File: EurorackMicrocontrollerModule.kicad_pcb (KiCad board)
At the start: 2 copper layers, 17.8 x 109.2 mm, 43 parts, among them J1 Teensy4.0_Pins_Right, J2 Teensy4.0_Pins_Left, J3 Conn_01x24_Male, J4 Conn_02x05_Counter_Clockwise, J5 Teensy4.0_Pins_Top, U1 PCM1754DBQ, U2 PCM1808PW, U3 AZ1117H2-ADJ

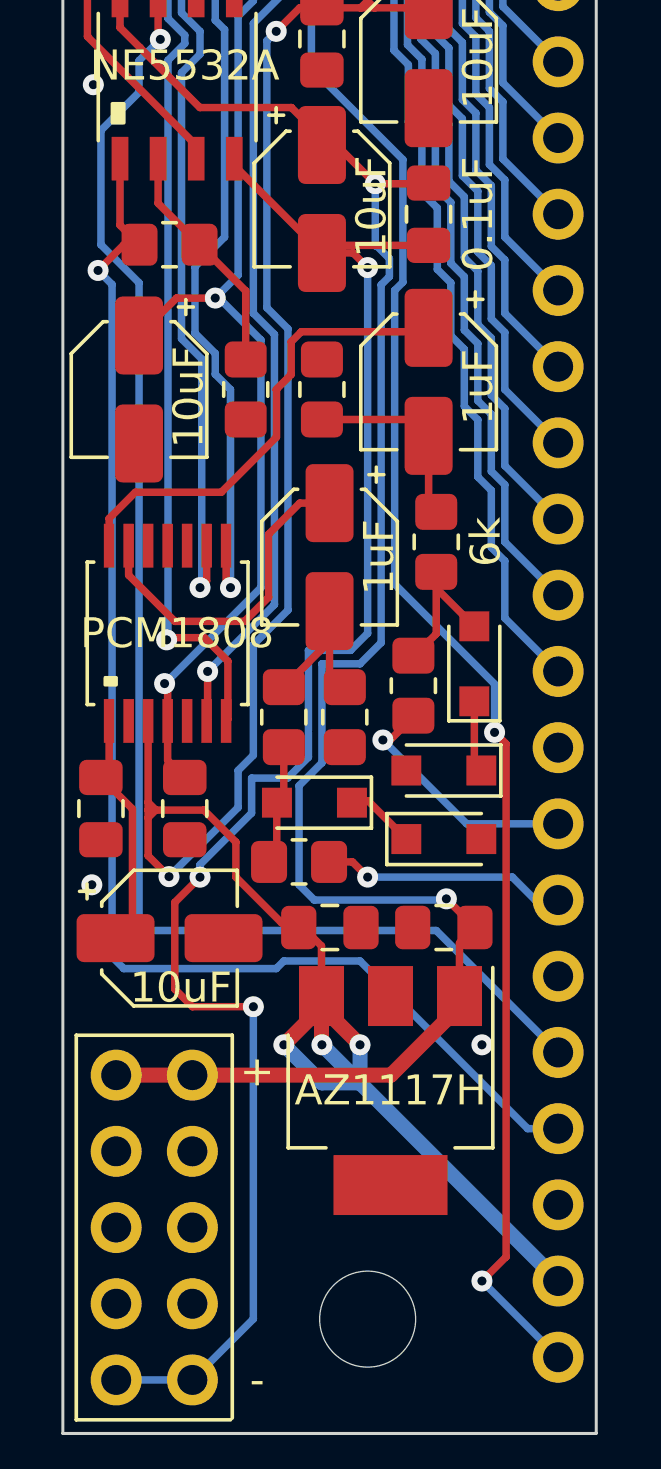
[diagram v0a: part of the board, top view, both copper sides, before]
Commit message: Changed LDO pad layout to a more common one
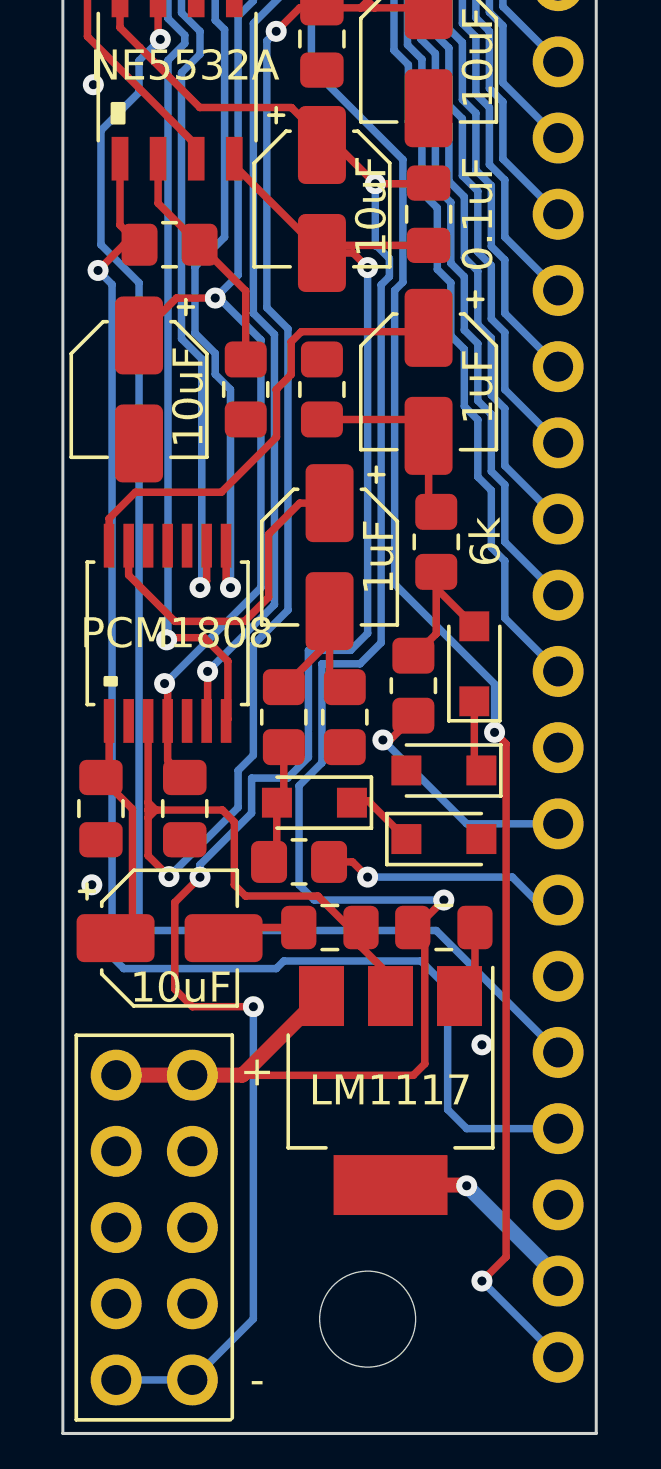
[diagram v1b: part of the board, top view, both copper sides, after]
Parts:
- U3: value AZ1117H2-ADJ -> LM1117-5.0
- turned C13 to 0 degrees
- turned C14 to 180 degrees
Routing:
- net +5V: track 114.4 -> 102.7 mm, vias 6 -> 4
- net GND: track 0.12 -> 5.62 mm
- net +12V: track 60.9 -> 64.6 mm
- net /5VPPAudioOutL: track 45.4 -> 47.8 mm

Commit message: Shortened PCB and moved top Screw hole; Added pin labels; Moved capacitor near power plug
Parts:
- moved REF** 10.2 mm to (162.6, 97.8)
- moved C10 6.54 mm to (156.3, 178.2), turned to 180 degrees
- moved C7 1.78 mm to (156.0, 174.8)
- moved C12 0.97 mm to (156.8, 171.3), turned to 0 degrees
- moved R9 0.89 mm to (161.2, 174.0)
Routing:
- net +5V: track 102.7 -> 110.5 mm, vias 4 -> 6
- net GND: track 5.62 -> 2.97 mm, vias 4 -> 3
- net -12V: track 56.6 -> 54.2 mm
- net Net-(C10-Pad2): track 8.02 -> 9.68 mm
- net /LAudioIn: track 8.42 -> 7.35 mm
- net /5VPPAudioOutR: track 50.4 -> 51.0 mm
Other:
- board size 17.8 x 109.2 mm -> 17.8 x 101.6 mm
- board text added: "3.3"
- board text added: "5"
- board text added: "LI"
- board text added: "LO"
- board text added: "RI"
- board text added: "RO"
